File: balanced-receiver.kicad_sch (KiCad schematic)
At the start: 51 parts, among them J1 NC3FAH2, J2 Barrel_Jack_Switch, J3 Screw_Terminal_01x02, J4 Screw_Terminal_01x02, J5 Screw_Terminal_01x02, J6 Screw_Terminal_01x02, J7 Screw_Terminal_01x02, J8 Conn_01x02_Pin, Q1 Q_PMOS_GDS, U1 THAT1240, U2 TPS62932, U3 LM2776

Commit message: Added DRC pipeline action
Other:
- company: Filip Tefr -> ${TITLE_BLOCK_AUTHOR}
- title: Balanced receiver -> ${TITLE_BLOCK_PROJECT_NAME}

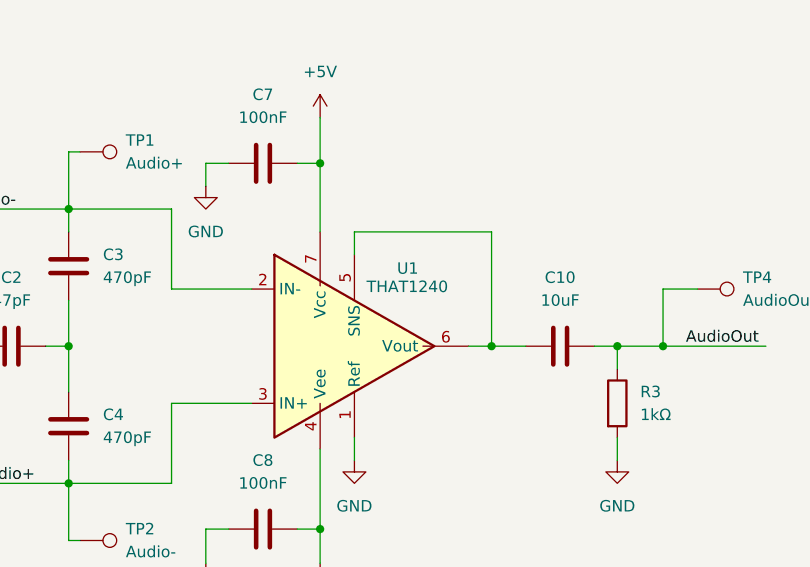
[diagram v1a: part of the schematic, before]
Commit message: Added local component library
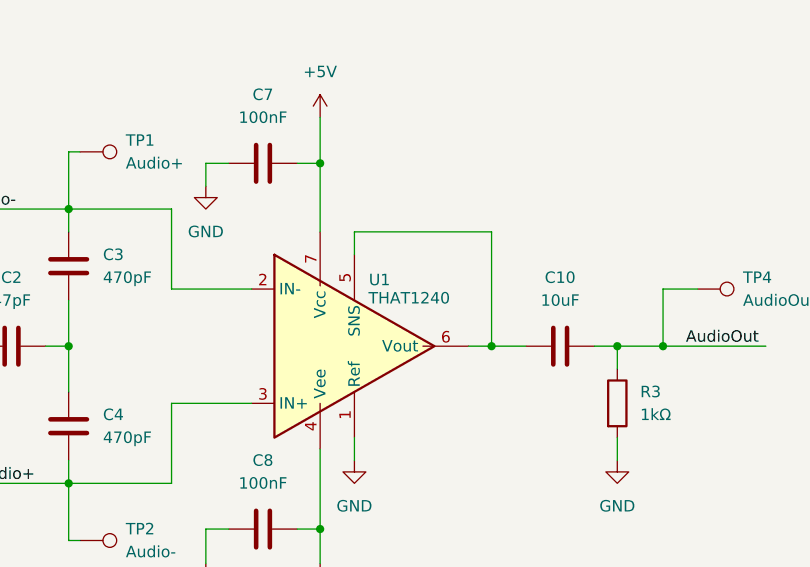
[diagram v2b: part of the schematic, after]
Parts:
- removed U1: THAT1240, Package_SO:SOIC-8_3.9x4.9mm_P1.27mm, symbol brbCZa-KicadSymLib:THAT1240
- added U1: THAT1240, Package_SO:SOIC-8_3.9x4.9mm_P1.27mm, symbol balanced-receiver:THAT1240
- F1: footprint brbCZa-KicadFootprintLib:Fuse_1812_4532Metric_Pad1.30x3.40mm_HandSolder -> balanced-receiver:Fuse_1812_4532Metric_Pad1.30x3.40mm_HandSolder
- J1: footprint brbCZa-KicadFootprintLib:Jack_XLR_Neutrik_NC3FAH2_Horizontal -> balanced-receiver:Jack_XLR_Neutrik_NC3FAH2_Horizontal
- J2: footprint brbCZa-KicadFootprintLib:BarrelJack_GCT_DCJ200-10-A_Horizontal -> balanced-receiver:BarrelJack_GCT_DCJ200-10-A_Horizontal
- J5: footprint brbCZa-KicadFootprintLib:JST_XH_B2B-XH-AM_1x02_P2.50mm_Vertical -> balanced-receiver:JST_XH_B2B-XH-AM_1x02_P2.50mm_Vertical
- L1: footprint brbCZa-KicadFootprintLib:L_7.3x7.3_H4.5 -> balanced-receiver:L_7.3x7.3_H4.5
- U2: footprint brbCZa-KicadFootprintLib:SOT-583-8 -> balanced-receiver:SOT-583-8
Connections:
- net +5V: now also U1.7 (Vcc)
- net -5V: now also U1.4 (Vee)
- net Audio+: now also U1.3 (IN+)
- net Audio-: now also U1.2 (IN-)
- net GND: now also U1.1 (Ref)
- net at C10.1: now also U1.5 (SNS), U1.6 (Vout)
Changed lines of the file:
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@@
 	)
 	(symbol
-		(lib_id "brbCZa-KicadSymLib:THAT1240")
-		(at 73.66 107.95 0)
-		(unit 1)
-		(exclude_from_sim no)
-		(in_bom yes)
-		(on_board yes)
-		(dnp no)
-		(property "Reference" "U1"
-			(at 82.042 99.314 0)
-			(effects
-				(font
-					(size 1.27 1.27)
-				)
-				(justify right)
-			)
-		)
-		(property "Value" "THAT1240"
-			(at 85.344 101.346 0)
-			(effects
-				(font
-					(size 1.27 1.27)
-				)
-				(justify right)
-			)
-		)
-		(property "Footprint" "Package_SO:SOIC-8_3.9x4.9mm_P1.27mm"
-			(at 74.93 107.95 0)
-			(effects
-				(font
-					(size 1.27 1.27)
-				)
-				(hide yes)
-			)
-		)
-		(property "Datasheet" "https://www.thatcorp.com/datashts/THAT_1240-Series_Datasheet.pdf"
-			(at 73.66 107.95 0)
-			(effects
-				(font
-					(size 1.27 1.27)
-				)
-				(hide yes)
-			)
-		)
-		(property "Description" "Precision differen-tial amplifiers designed primarily for use as balanced line receivers for audio applications"
-			(at 74.93 107.95 0)
-			(effects
-				(font
-					(size 1.27 1.27)
-				)
-				(hide yes)
-			)
-		)
-		(property "LCSC" "1240S08-U "
-			(at 73.66 107.95 0)
-			(effects
-				(font
-					(size 1.27 1.27)
-				)
-				(hide yes)
-			)
-		)
-		(property "Sim.Device" ""
-			(at 73.66 107.95 0)
-			(effects
-				(font
-					(size 1.27 1.27)
-				)
-				(hide yes)
-			)
-		)
-		(property "Sim.Pins" ""
-			(at 73.66 107.95 0)
-			(effects
-				(font
-					(size 1.27 1.27)
-				)
-				(hide yes)
-			)
-		)
-		(pin "6"
-		)
-		(pin "2"
-		)
-		(pin "5"
-		)
-		(pin "4"
-		)
-		(pin "3"
-		)
-		(pin "1"
-		)
-		(pin "7"
-		)
-		(instances
-			(project ""
-				(path "/6a415962-4bc6-46b3-a4a9-4a4125d0fb6a"
-					(reference "U1")
-					(unit 1)
-				)
-			)
-		)
-	)
-	(symbol
 		(lib_id "Device:C_Polarized")
 		(at 154.94 39.37 0)
@@
 			)
 		)
-		(property "Footprint" "brbCZa-KicadFootprintLib:Fuse_1812_4532Metric_Pad1.30x3.40mm_HandSolder"
+		(property "Footprint" "balanced-receiver:Fuse_1812_4532Metric_Pad1.30x3.40mm_HandSolder"
 			(at 171.45 151.13 0)
 			(effects
@@
 			)
 		)
-		(property "Footprint" "brbCZa-KicadFootprintLib:SOT-583-8"
+		(property "Footprint" "balanced-receiver:SOT-583-8"
 			(at 109.22 66.04 0)
 			(effects
@@
 			)
 		)
-		(property "Footprint" "brbCZa-KicadFootprintLib:BarrelJack_GCT_DCJ200-10-A_Horizontal"
+		(property "Footprint" "balanced-receiver:BarrelJack_GCT_DCJ200-10-A_Horizontal"
 			(at 82.55 164.846 0)
 			(effects
@@
 			)
 		)
-		(property "Footprint" "brbCZa-KicadFootprintLib:JST_XH_B2B-XH-AM_1x02_P2.50mm_Vertical"
+		(property "Footprint" "balanced-receiver:JST_XH_B2B-XH-AM_1x02_P2.50mm_Vertical"
 			(at 245.11 116.84 0)
 			(effects
@@
 			)
 		)
-		(property "Footprint" "brbCZa-KicadFootprintLib:Jack_XLR_Neutrik_NC3FAH2_Horizontal"
+		(property "Footprint" "balanced-receiver:Jack_XLR_Neutrik_NC3FAH2_Horizontal"
 			(at 40.64 157.48 0)
 			(effects
@@
 			)
 		)
-		(property "Footprint" "brbCZa-KicadFootprintLib:L_7.3x7.3_H4.5"
+		(property "Footprint" "balanced-receiver:L_7.3x7.3_H4.5"
 			(at 137.16 33.02 0)
 			(effects
@@
 					(unit 1)
 				)
+			)
+		)
+	)
+	(symbol
+		(lib_id "balanced-receiver:THAT1240")
+		(at 73.66 107.95 0)
+		(unit 1)
+		(exclude_from_sim no)
+		(in_bom yes)
+		(on_board yes)
+		(dnp no)
+		(property "Reference" "U1"
+			(at 77.724 100.584 0)
+			(effects
+				(font
+					(size 1.27 1.27)
+				)
+			)
+		)
+		(property "Value" "THAT1240"
+			(at 81.026 102.616 0)
+			(effects
+				(font
+					(size 1.27 1.27)
+				)
+			)
+		)
+		(property "Footprint" "Package_SO:SOIC-8_3.9x4.9mm_P1.27mm"
+			(at 74.93 107.95 0)
+			(effects
+				(font
+					(size 1.27 1.27)
+				)
+				(hide yes)
+			)
+		)
+		(property "Datasheet" "https://www.thatcorp.com/datashts/THAT_1240-Series_Datasheet.pdf"
+			(at 73.66 107.95 0)
+			(effects
+				(font
+					(size 1.27 1.27)
+				)
+				(hide yes)
+			)
+		)
+		(property "Description" "Precision differential amplifiers designed primarily for use as balanced line receivers for audio applications"
+			(at 74.93 107.95 0)
+			(effects
+				(font
+					(size 1.27 1.27)
+				)
+				(hide yes)
+			)
+		)
+		(pin "4"
+		)
+		(pin "7"
+		)
+		(pin "2"
+		)
+		(pin "1"
+		)
+		(pin "3"
+		)
+		(pin "6"
+		)
+		(pin "5"
+		)
+		(instances
+			(project ""
+				(path "/6a415962-4bc6-46b3-a4a9-4a4125d0fb6a"
+					(reference "U1")
+					(unit 1)
+				)

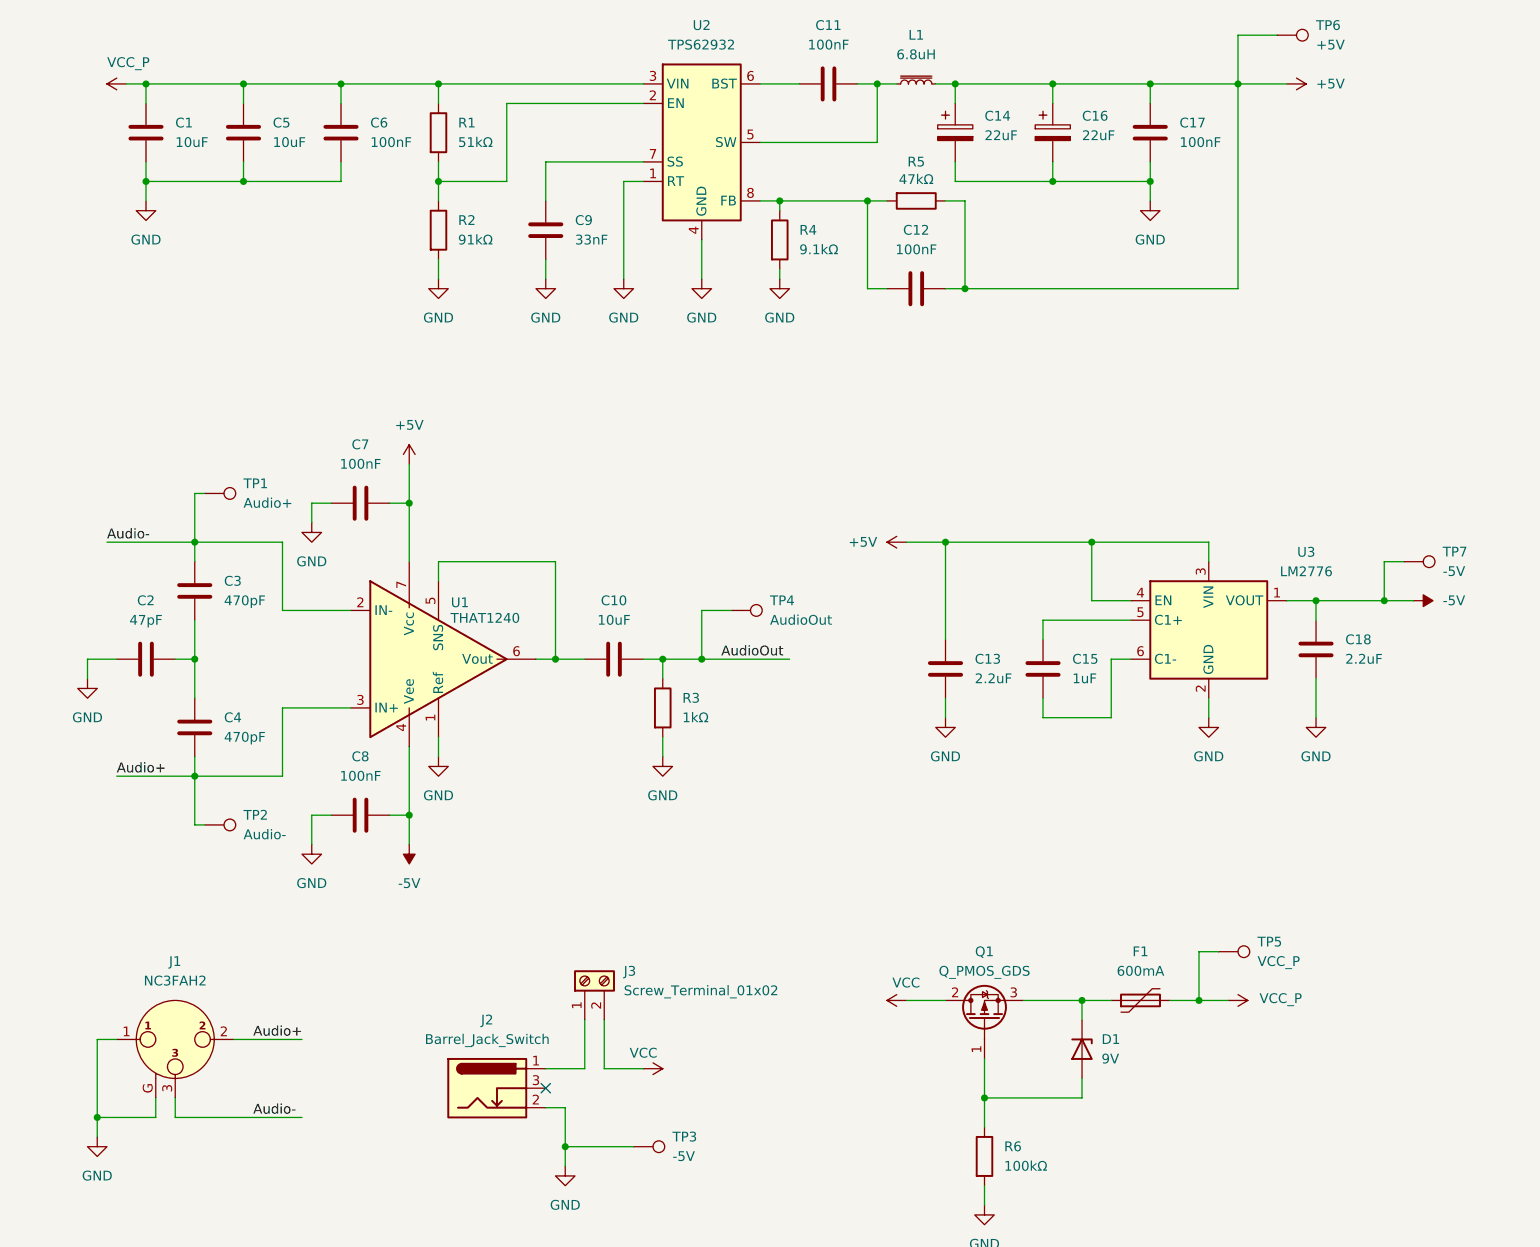
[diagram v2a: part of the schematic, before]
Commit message: Fixed DRC and ERC errors
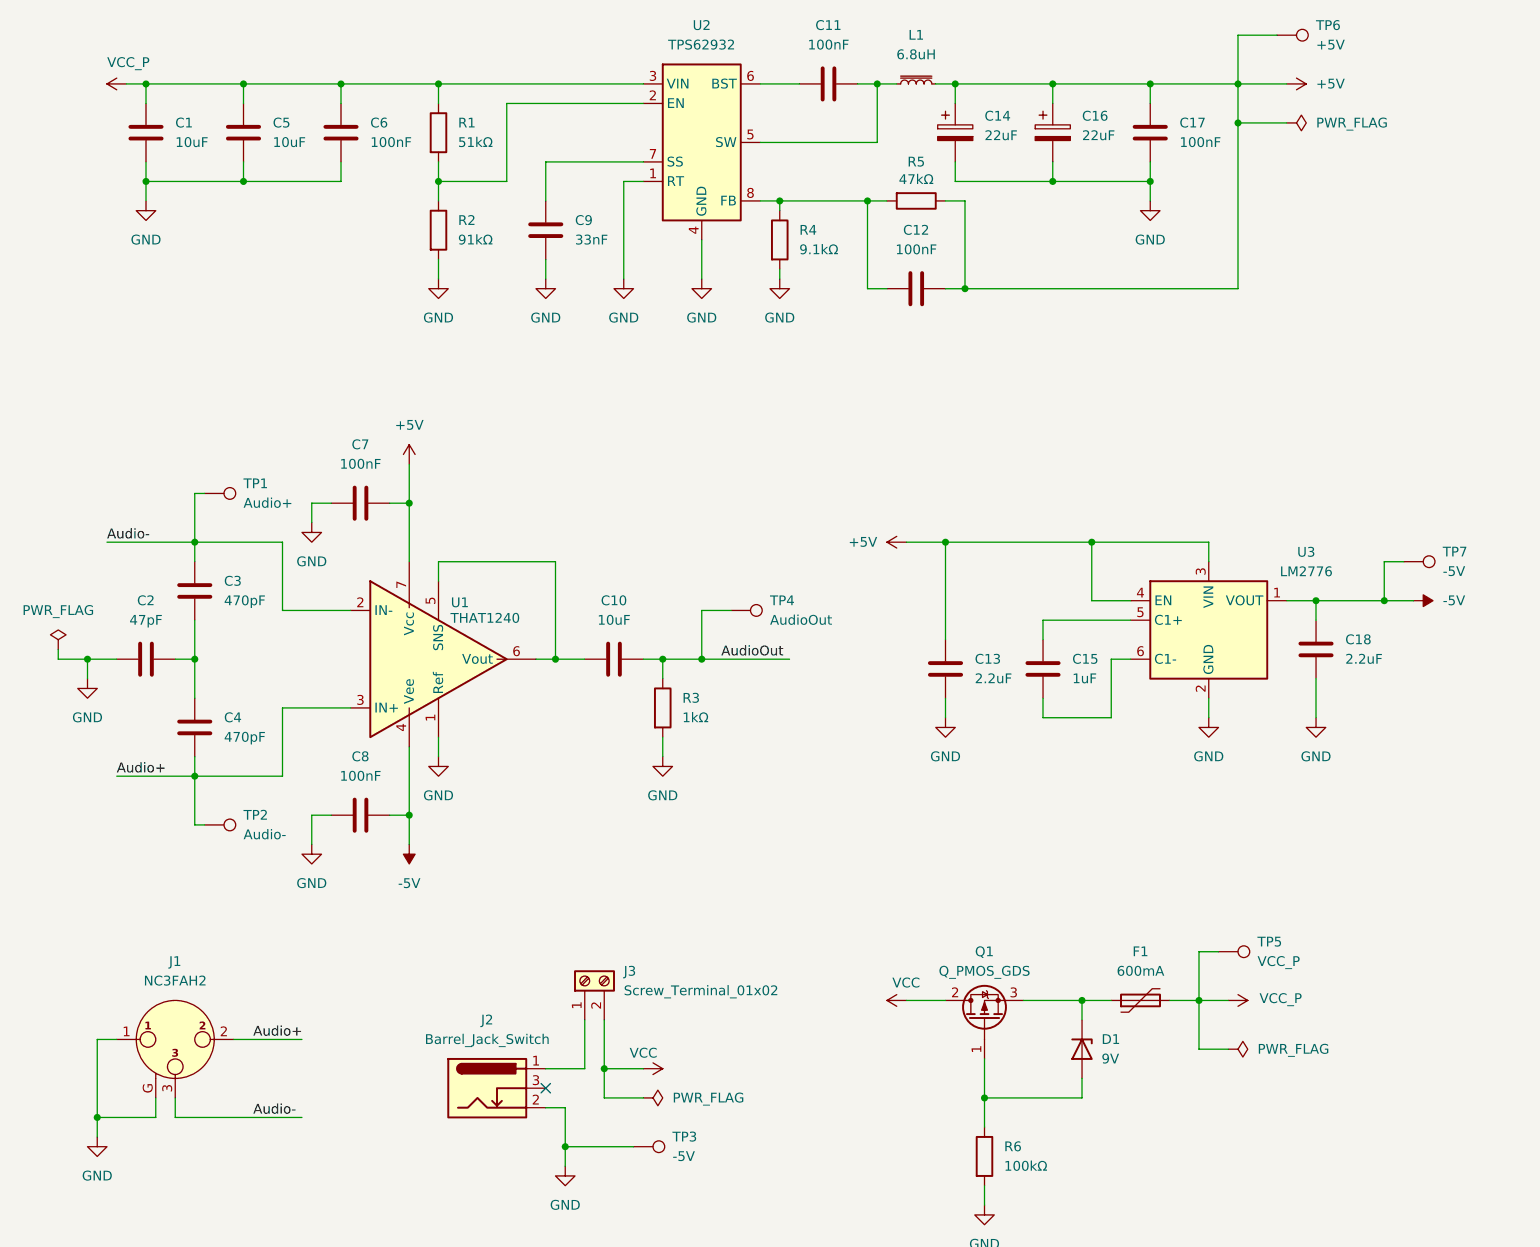
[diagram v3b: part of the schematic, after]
